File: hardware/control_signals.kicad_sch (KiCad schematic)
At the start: 25 parts, among them Q10 BC557, Q11 BC557, Q12 BC547, Q9 BC557, U8 74LS06N

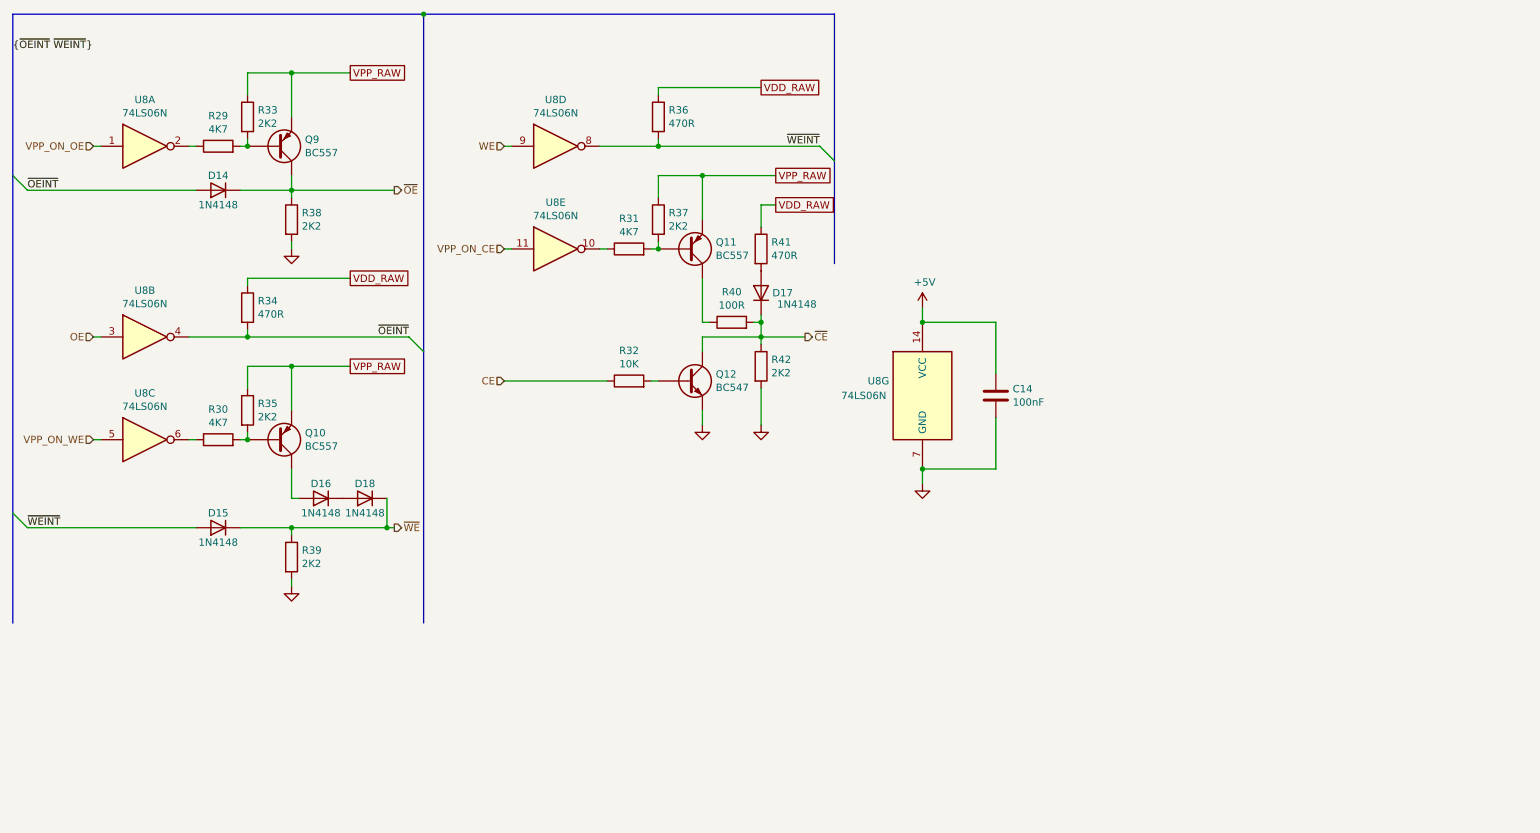
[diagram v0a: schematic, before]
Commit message: Rev.E. Updated hardware design.
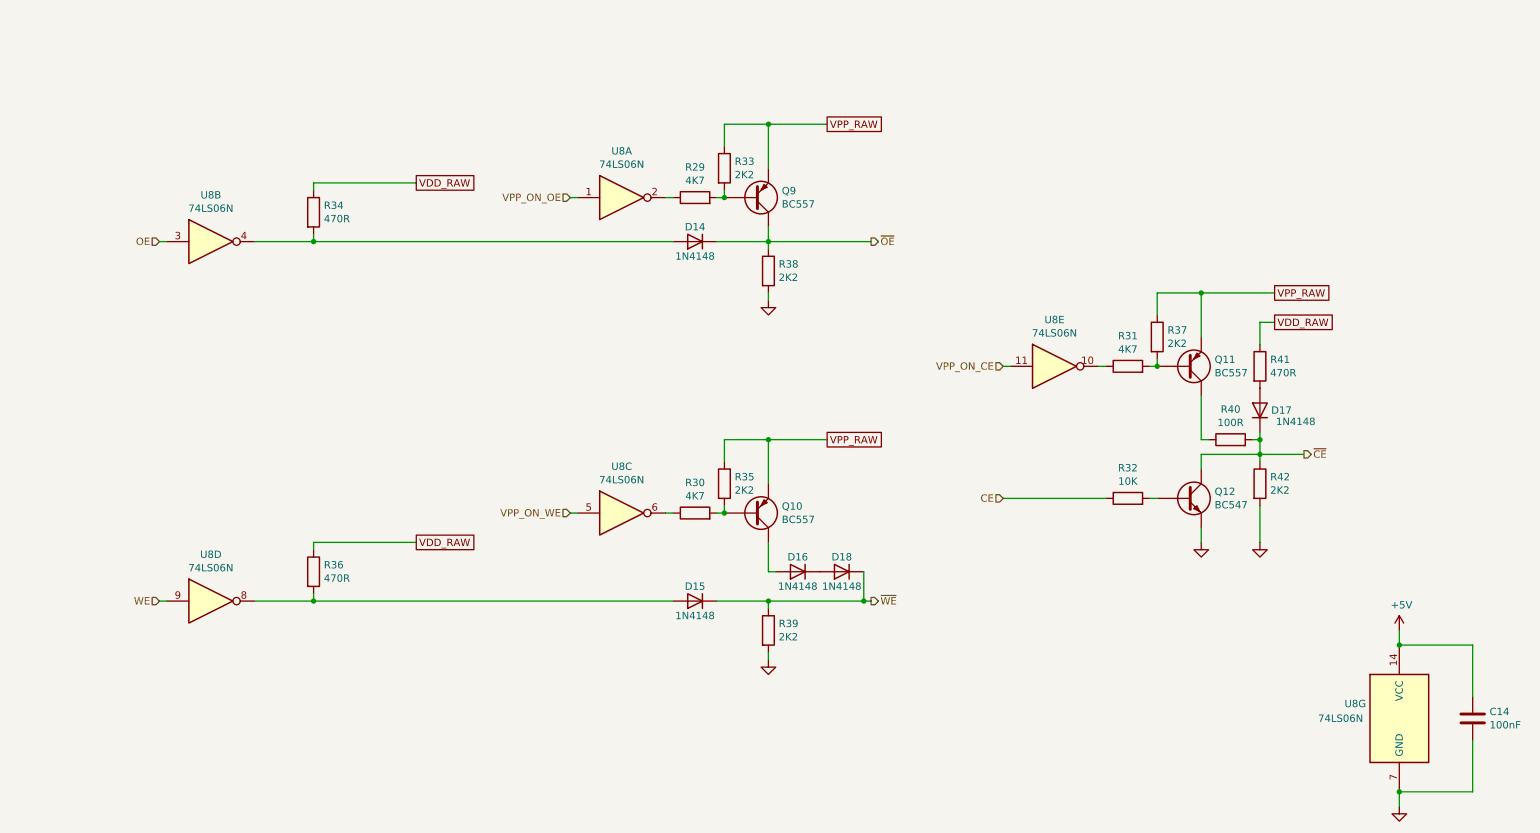
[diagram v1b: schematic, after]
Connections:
- net ~{OEINT}: no longer names the net of D14.2 (A), R34.2, U8.4
- net ~{WEINT}: no longer names the net of D15.2 (A), R36.2, U8.8
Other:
- moved on the sheet: C14, D14, D15, D16, D17, D18, Q10, Q11, Q12, Q9, R29, R30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

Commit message: Rev.E. Updated specifications document and hardware design.
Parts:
- Q10, Q11, Q9: value BC557 -> (none); footprint Package_TO_SOT_THT:TO-92_Inline_Wide -> (none)
- Q12: value BC547 -> (none); footprint Package_TO_SOT_THT:TO-92_Inline_Wide -> (none)
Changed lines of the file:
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@@
       (effects (font (size 1.27 1.27)) (justify left))
     )
-    (property "Value" "BC557" (id 1) (at 149.6314 49.403 0)
-      (effects (font (size 1.27 1.27)) (justify left))
-    )
-    (property "Footprint" "Package_TO_SOT_THT:TO-92_Inline_Wide" (id 2) (at 149.86 46.355 0)
+    (property "Value" "" (id 1) (at 149.6314 49.403 0)
+      (effects (font (size 1.27 1.27)) (justify left))
+    )
+    (property "Footprint" "" (id 2) (at 149.86 46.355 0)
       (effects (font (size 1.27 1.27) italic) (justify left) hide)
     )
@@
       (effects (font (size 1.27 1.27)) (justify left))
     )
-    (property "Value" "BC557" (id 1) (at 149.6314 104.013 0)
-      (effects (font (size 1.27 1.27)) (justify left))
-    )
-    (property "Footprint" "Package_TO_SOT_THT:TO-92_Inline_Wide" (id 2) (at 149.86 100.965 0)
+    (property "Value" "" (id 1) (at 149.6314 104.013 0)
+      (effects (font (size 1.27 1.27)) (justify left))
+    )
+    (property "Footprint" "" (id 2) (at 149.86 100.965 0)
       (effects (font (size 1.27 1.27) italic) (justify left) hide)
     )
@@
       (effects (font (size 1.27 1.27)) (justify left))
     )
-    (property "Value" "BC557" (id 1) (at 224.5614 78.613 0)
-      (effects (font (size 1.27 1.27)) (justify left))
-    )
-    (property "Footprint" "Package_TO_SOT_THT:TO-92_Inline_Wide" (id 2) (at 224.79 75.565 0)
+    (property "Value" "" (id 1) (at 224.5614 78.613 0)
+      (effects (font (size 1.27 1.27)) (justify left))
+    )
+    (property "Footprint" "" (id 2) (at 224.79 75.565 0)
       (effects (font (size 1.27 1.27) italic) (justify left) hide)
     )
@@
       (effects (font (size 1.27 1.27)) (justify left))
     )
-    (property "Value" "BC547" (id 1) (at 224.5614 101.473 0)
-      (effects (font (size 1.27 1.27)) (justify left))
-    )
-    (property "Footprint" "Package_TO_SOT_THT:TO-92_Inline_Wide" (id 2) (at 224.79 102.235 0)
+    (property "Value" "" (id 1) (at 224.5614 101.473 0)
+      (effects (font (size 1.27 1.27)) (justify left))
+    )
+    (property "Footprint" "" (id 2) (at 224.79 102.235 0)
       (effects (font (size 1.27 1.27) italic) (justify left) hide)
     )

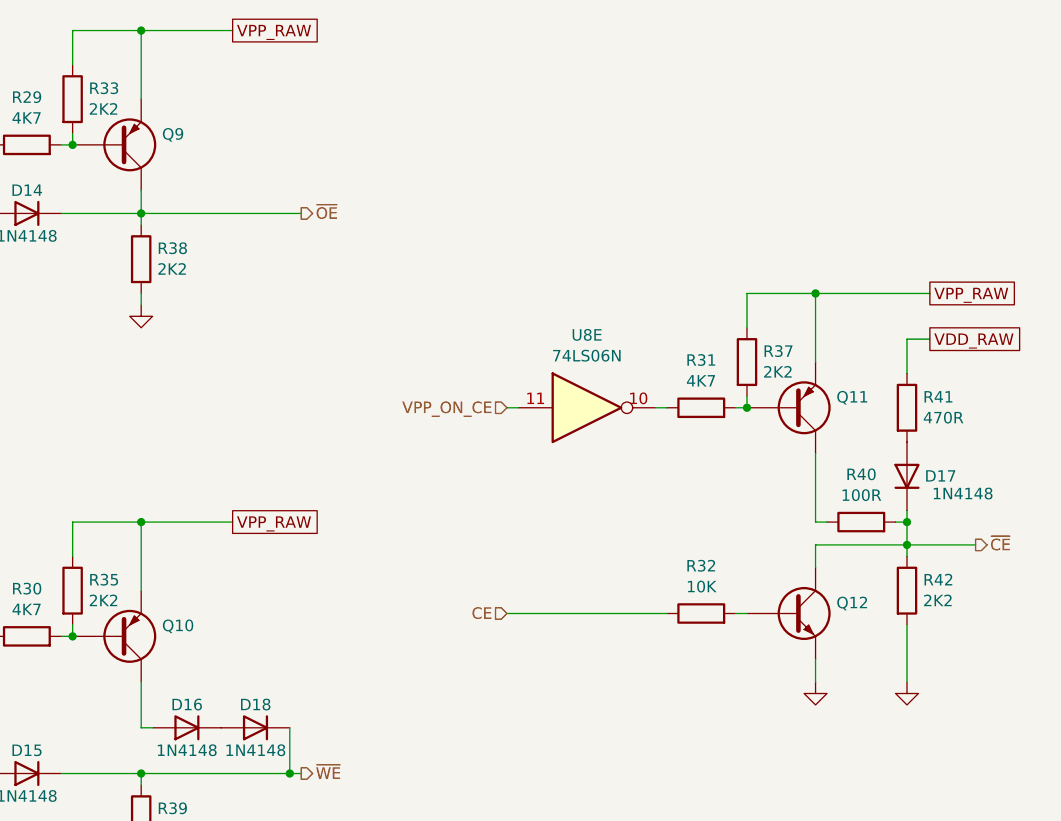
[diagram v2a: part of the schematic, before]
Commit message: Rev.E. Updated R51 wattage.
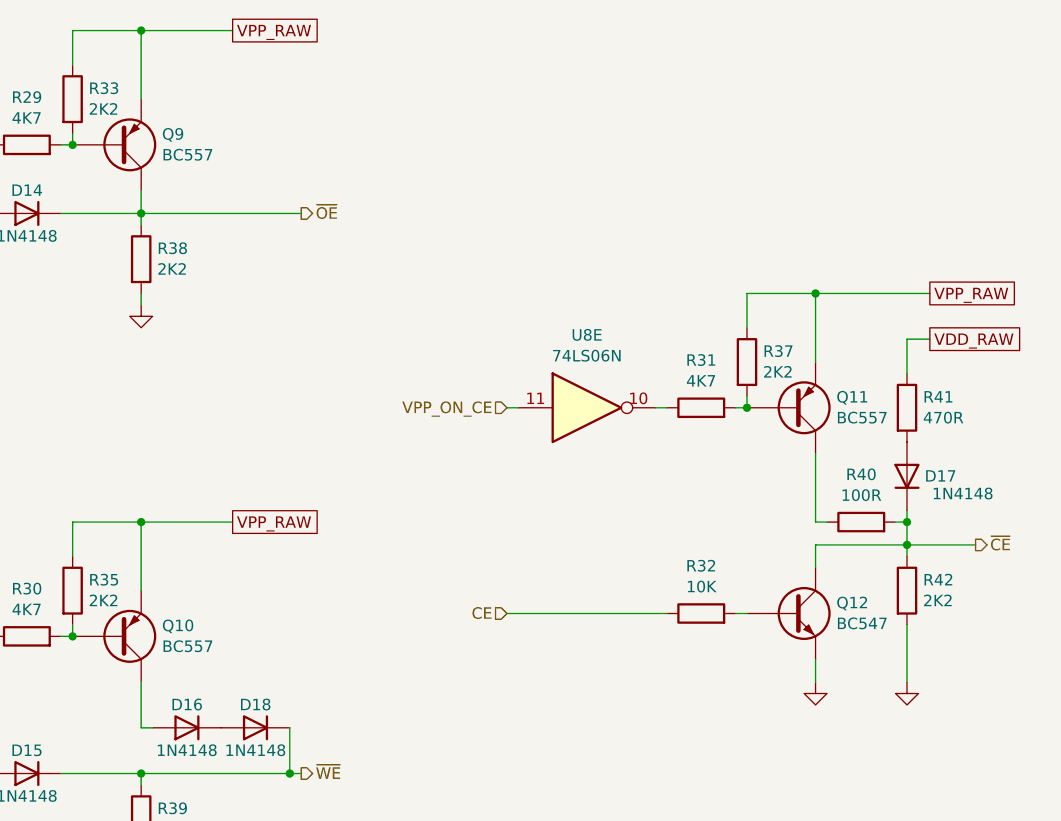
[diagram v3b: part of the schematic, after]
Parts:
- Q10, Q11, Q9: value (none) -> BC557; footprint (none) -> Package_TO_SOT_THT:TO-92_Inline_Wide
- Q12: value (none) -> BC547; footprint (none) -> Package_TO_SOT_THT:TO-92_Inline_Wide
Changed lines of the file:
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@@
       (effects (font (size 1.27 1.27)) (justify left))
     )
-    (property "Value" "" (id 1) (at 149.6314 49.403 0)
-      (effects (font (size 1.27 1.27)) (justify left))
-    )
-    (property "Footprint" "" (id 2) (at 149.86 46.355 0)
+    (property "Value" "BC557" (id 1) (at 149.6314 49.403 0)
+      (effects (font (size 1.27 1.27)) (justify left))
+    )
+    (property "Footprint" "Package_TO_SOT_THT:TO-92_Inline_Wide" (id 2) (at 149.86 46.355 0)
       (effects (font (size 1.27 1.27) italic) (justify left) hide)
     )
@@
       (effects (font (size 1.27 1.27)) (justify left))
     )
-    (property "Value" "" (id 1) (at 149.6314 104.013 0)
-      (effects (font (size 1.27 1.27)) (justify left))
-    )
-    (property "Footprint" "" (id 2) (at 149.86 100.965 0)
+    (property "Value" "BC557" (id 1) (at 149.6314 104.013 0)
+      (effects (font (size 1.27 1.27)) (justify left))
+    )
+    (property "Footprint" "Package_TO_SOT_THT:TO-92_Inline_Wide" (id 2) (at 149.86 100.965 0)
       (effects (font (size 1.27 1.27) italic) (justify left) hide)
     )
@@
       (effects (font (size 1.27 1.27)) (justify left))
     )
-    (property "Value" "" (id 1) (at 224.5614 78.613 0)
-      (effects (font (size 1.27 1.27)) (justify left))
-    )
-    (property "Footprint" "" (id 2) (at 224.79 75.565 0)
+    (property "Value" "BC557" (id 1) (at 224.5614 78.613 0)
+      (effects (font (size 1.27 1.27)) (justify left))
+    )
+    (property "Footprint" "Package_TO_SOT_THT:TO-92_Inline_Wide" (id 2) (at 224.79 75.565 0)
       (effects (font (size 1.27 1.27) italic) (justify left) hide)
     )
@@
       (effects (font (size 1.27 1.27)) (justify left))
     )
-    (property "Value" "" (id 1) (at 224.5614 101.473 0)
-      (effects (font (size 1.27 1.27)) (justify left))
-    )
-    (property "Footprint" "" (id 2) (at 224.79 102.235 0)
+    (property "Value" "BC547" (id 1) (at 224.5614 101.473 0)
+      (effects (font (size 1.27 1.27)) (justify left))
+    )
+    (property "Footprint" "Package_TO_SOT_THT:TO-92_Inline_Wide" (id 2) (at 224.79 102.235 0)
       (effects (font (size 1.27 1.27) italic) (justify left) hide)
     )
